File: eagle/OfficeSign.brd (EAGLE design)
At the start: 127.1 x 39.4 mm, 71 parts, among them Q1 16MHZ, SW3 KMR2, SW4 KMR2, U1 ATMEGA328, U2 L7805CDT-TR, U3 NCS36000, U4 PIR, U5 WS2801, U6 SPX3819, U8 TXB0108PWR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

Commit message: Move Files Around
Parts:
- removed U$10: FIDUCIAL, adafruit:FIDUCIAL_1MM
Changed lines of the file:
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@@
 <attribute name="SPICEPREFIX" value="C" x="46.355" y="27.178" size="1.778" layer="27" rot="R270" display="off"/>
 </element>
-<element name="U$10" library="adafruit" package="FIDUCIAL_1MM" value="FIDUCIAL" x="45.085" y="19.304"/>
 </elements>
 <signals>

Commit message: WIP
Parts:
- removed D11: MBR120, microbuilder:SOD-123
- added D2: MBR120, microbuilder:SOD-123
- moved D10 4.71 mm to (24.1, 32.0), turned to 90 degrees
- moved C16 1.80 mm to (43.8, 25.4), turned to 90 degrees
- moved C17 1.78 mm to (46.4, 25.4), turned to 90 degrees
- moved R10 0.80 mm to (125.5, 21.8)
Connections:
- net STROBE renamed D2
- removed net D5: U1.9
- removed net D6: U1.10
- removed net GPIO4: X2.13
- removed net GPIO5: X2.14
- removed net N$17: C15.1, D10.C, D11.C, R21.1, U6.1
- removed net RST7: U1.1
- removed net VBAT: D11.A
- new net N$23: C15.1, D10.C, D2.C, R21.1, U6.1
- new net OCC: U1.9, U8.15
- new net OCC_ESP: U8.6, X2.13
- new net RES: U1.10, U8.14
- new net RES_ESP: U8.7, X2.14
- net OUT: now also U1.1
- net VCC: now also D2.A
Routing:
- net N$23: track 0.00 -> 23.2 mm
- net N$17: track 22.2 -> 0.00 mm
- net VIN: track 29.8 -> 13.2 mm
- net GND: track 0.90 -> 0.00 mm
- net VBAT: track 0.54 -> 0.00 mm

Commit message: Moves and Shakes
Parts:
- added POT: (no value), SparkFun-Connectors:JST-4-PTH
- added R15: 3.3, adafruit:M0805
- added U7: NJVMJD2955T4G, bg_eagle_lib:DPAK
- C19: value 10uF -> 0.33uF
- moved JP1 10.2 mm to (76.6, 1.52)
- moved C2 8.98 mm to (86.9, 14.2)
- moved C19 8.89 mm to (96.9, 21.0)
- moved Q1 8.68 mm to (93.4, 29.8)
- moved C3 8.27 mm to (92.8, 25.7)
- moved R6 7.11 mm to (77.9, 32.3)
- moved R2 6.18 mm to (86.9, 19.1), turned to 90 degrees
- moved U1 5.91 mm to (84.3, 28.3)
- moved S1 5.86 mm to (80.1, 19.6)
- moved C1 4.83 mm to (77.6, 30.0)
- moved U2 3.31 mm to (101.6, 18.9)
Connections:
- new net N$24: POT.3
- new net N$25: POT.2
- new net N$26: JP4.PWR, R15.2, U7.3
- net GND: now also POT.1
- net RAW: now also R15.1, U7.1; no longer JP4.PWR
- net VCC: now also POT.4, U7.4

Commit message: Add Indicator
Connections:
- removed net A1: U1.24
- removed net N$24: POT.3
- new net POT: POT.3, U1.24
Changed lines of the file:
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@@
 <?xml version="1.0" encoding="utf-8"?>
 <!DOCTYPE eagle SYSTEM "eagle.dtd">
-<eagle version="8.7.0">
+<eagle version="8.7.1">
 <drawing>
 <settings>
@@
 <contactref element="U1" pad="13"/>
 </signal>
-<signal name="A1">
+<signal name="POT">
 <contactref element="U1" pad="24"/>
+<contactref element="POT" pad="3"/>
+<wire x1="97.012" y1="6.096" x2="79.312771875" y2="29.376425" width="0" layer="19" extent="1-1"/>
 </signal>
 <signal name="D4">
@@
 <wire x1="24.13" y1="30.154" x2="26.416" y2="30.154" width="0.4064" layer="1"/>
 </signal>
-<signal name="N$24">
-<contactref element="POT" pad="3"/>
-</signal>
 <signal name="N$25">

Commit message: wip
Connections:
- net D2 renamed POD_IND
- net N$25 renamed POT_IND
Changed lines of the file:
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@@
 <wire x1="48.0028" y1="18.329" x2="88.7775375" y2="29.9421125" width="0" layer="19" extent="1-1"/>
 </signal>
-<signal name="D2">
+<signal name="POD_IND">
 <contactref element="U1" pad="32"/>
 </signal>
@@
 <wire x1="24.13" y1="30.154" x2="26.416" y2="30.154" width="0.4064" layer="1"/>
 </signal>
-<signal name="N$25">
+<signal name="POT_IND">
 <contactref element="POT" pad="2"/>
 </signal>

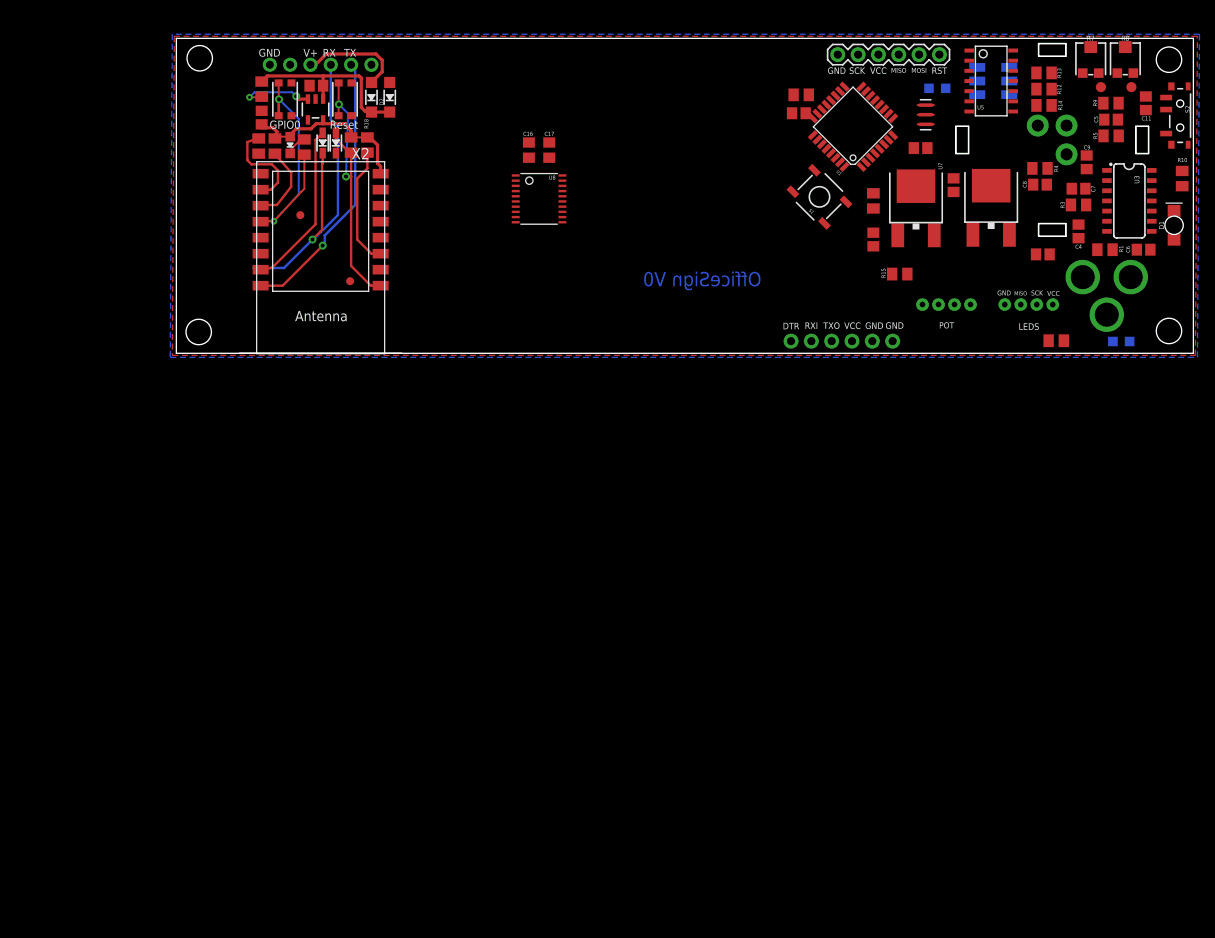
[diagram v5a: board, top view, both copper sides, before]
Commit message: Add Remote Motion / Work on Dispaly
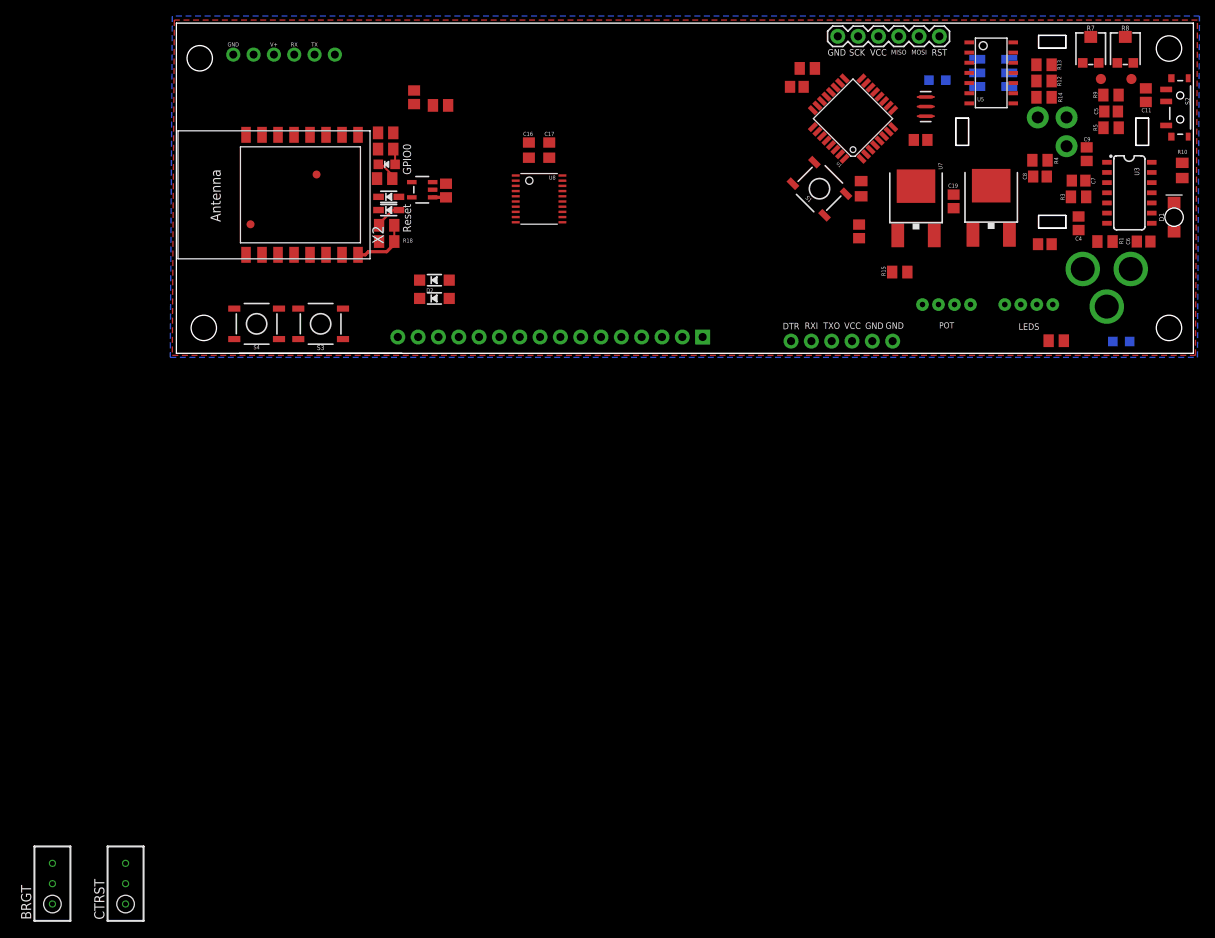
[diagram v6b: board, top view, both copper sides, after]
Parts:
- removed SW3, SW4: KMR2, microbuilder:BTN_KMR2_4.6X2.8
- added BRGT: 1K, resistor:RTRIM3296W
- added CTRST: 10K, resistor:RTRIM3296W
- added S3: Reset, SparkFun-Switches:TACTILE_SWITCH_SMD_5.2MM
- added S4: GPIO0, SparkFun-Switches:TACTILE_SWITCH_SMD_5.2MM
- added U9: LCD-16X2NOHOLES, SparkFun-Displays:LCD-16X2_NOHOLES
- S1: device Testing:TACTILE-SWITCH-SMD-ALT01 -> SparkFun-Switches:TACTILE_SWITCH_SMD_5.2MM
- moved D2 25.8 mm to (32.0, 6.86), turned to 0 degrees
- moved D10 24.2 mm to (32.0, 9.14), turned to 0 degrees
- moved R21 22.4 mm to (32.8, 31.0), turned to 180 degrees
- moved U$34 21.3 mm to (7.49, 28.7), turned to 270 degrees
- moved C15 20.8 mm to (33.5, 20.3), turned to 90 degrees
- moved C14 19.2 mm to (29.5, 32.0)
- moved U6 16.7 mm to (30.5, 20.4), turned to 90 degrees
- moved R20 16.0 mm to (25.9, 27.6), turned to 0 degrees
- moved FID2 14.3 mm to (9.02, 16.1), turned to 90 degrees
- moved R22 13.8 mm to (25.9, 25.5), turned to 0 degrees
- moved D12 12.3 mm to (26.0, 23.6), turned to 90 degrees
- moved R18 12.3 mm to (26.0, 14.0), turned to 0 degrees
- moved R19 11.0 mm to (26.0, 16.0), turned to 0 degrees
- moved R23 10.8 mm to (25.8, 21.8), turned to 0 degrees
- moved D8 10.7 mm to (26.3, 17.9), turned to 0 degrees
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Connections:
- net POD_IND renamed D2
- removed net N$26: JP4.PWR, R15.2, U7.3
- removed net POT_IND: POT.2
- removed net SSRX: U1.12
- new net A1: BRGT.2, U9.15
- new net DB4: U9.11
- new net DB5: U9.12
- new net DB6: U9.13
- new net DB7: U9.14
- new net E: U9.6
- new net L7805_IN: C19.1, R15.1, U2.1, U7.1
- new net POT_LED: POT.2, U1.1
- new net RS: U9.4
- new net VO: CTRST.2, U9.3
- net GND: now also CTRST.1, S3.1, S3.2, S4.1, S4.2, U9.1, U9.16, U9.5; no longer SW3.A, SW3.A', SW4.A, SW4.A'
- net GPIO0: now also S4.3, S4.4; no longer SW4.B, SW4.B'
- net OUT: now also U1.12; no longer U1.1
- net RAW: now also JP4.PWR, R15.2, U7.3; no longer C19.1, LEDS.4, R15.1, U2.1, U7.1
- net RESET_HZA: now also S3.3, S3.4; no longer SW3.B, SW3.B'
- net VCC: now also BRGT.3, CTRST.3, LEDS.4, U9.2
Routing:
- net RXD_5V: track 43.8 -> 0.00 mm, vias 1 -> 0
- net GPIO0: track 35.2 -> 0.00 mm, vias 2 -> 0
- net TXD: track 35.3 -> 1.02 mm, vias 1 -> 0
- net RESET_HZA: track 36.5 -> 3.38 mm, vias 2 -> 0
- net N$23: track 23.2 -> 1.67 mm
- net RXD: track 20.9 -> 0.00 mm
- net CH_PD: track 15.0 -> 0.00 mm
- net 3.3V: track 23.0 -> 9.48 mm
- net VIN: track 13.2 -> 0.00 mm
- net GPIO15: track 12.0 -> 0.00 mm
- net GPIO2: track 9.75 -> 0.00 mm
- net LDO_EN: track 9.46 -> 0.00 mm, vias 2 -> 0
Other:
- board size 127.1 x 39.4 mm -> 127.1 x 41.3 mm
- board text added: "LED"
- board text added: "LED MAX: 1.5A"
- board text added: "LEDS"
- board text added: "POT"
- board text added: "VCC: 9-12V"
- board text removed: "OfficeSign V0"

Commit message: Add Display / Add Indicator LEDs
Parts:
- removed D12: RED, microbuilder:CHIPLED_0805_NOOUTLINE
- added D4: Green, led:CHIPLED_0805
- added D5: Red, led:CHIPLED_0805
- added LED3: RED, led:CHIP-LED0805
- added R16: 1k, adafruit:M0805
- added R17: 300, adafruit:M0805
- D1: device SparkFun-LED:LED-1206-BOTTOM -> led:CHIPLED_0805
- D3, LED1: device adafruit:CHIPLED_0805 -> led:CHIPLED_0805
- moved CTRST 113.8 mm to (79.0, 8.64), turned to 270 degrees
- moved BRGT 95.4 mm to (42.9, 8.89), turned to 90 degrees
- moved FRAME1 65.2 mm to (48.3, -53.3)
- moved JP1 38.3 mm to (72.3, 39.6), turned to 0 degrees
- moved U9 16.8 mm to (50.3, -13.7)
- moved D1 5.98 mm to (123.2, 22.9), flipped to the bottom, turned to 0 degrees
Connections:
- removed net DB4: U9.11
- removed net DB5: U9.12
- removed net DB6: U9.13
- removed net DB7: U9.14
- removed net GPIO12: X2.6
- removed net GPIO13: X2.7
- removed net GPIO14: X2.5
- removed net GPIO15: R20.2, X2.10
- removed net GPIO16: X2.4
- removed net GPIO2: R22.1, X2.11
- removed net RS: U9.4
- new net E_ESP: R22.1, U8.3, X2.11
- new net LCD4_ESP: U8.4, X2.4
- new net LCD5_ESP: U8.5, X2.5
- new net LCD6_ESP: U8.6, X2.6
- new net LCD7_ESP: U8.7, X2.7
- new net LCD_D4: U8.17, U9.11
- new net LCD_D5: U8.16, U9.12
- new net LCD_D6: U8.15, U9.13
- new net LCD_D7: U8.14, U9.14
- new net LCD_E: U9.6
- new net LCD_RS: U8.20, U9.4
- new net N$17: LED3.C, R23.2
- new net N$24: D4.C, R16.2
- new net RS_ESP: R20.2, U8.1, X2.10
- net 3.3V: now also LED3.A; no longer D12.A
- net E: now also U8.18; no longer U9.6
- net GND: now also R16.1, R17.1
- net N$18: now also D5.C, R17.2; no longer D12.C, R23.2
- net OCC: now also D4.A, U8.13; no longer U8.15
- net OCC_ESP: now also U8.8; no longer U8.6
- net RES: now also U8.12; no longer U8.14
- net RES_ESP: now also D5.A, U8.9; no longer U8.7
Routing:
- net N$18: track 3.22 -> 0.00 mm
- net 3.3V: track 9.48 -> 8.06 mm
- net LCD5_ESP: track 0.00 -> 0.83 mm
- net GPIO14: track 0.83 -> 0.00 mm

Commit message: Screen is plugged in but doesnt work
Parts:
- R15: value 3.3 -> 22
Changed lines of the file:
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@@
 <attribute name="VALUE" x="88.646" y="16.618" size="0.508" layer="27" rot="R90"/>
 </element>
-<element name="R15" library="adafruit" package="M0805" value="3.3" x="90.17" y="10.16" smashed="yes">
+<element name="R15" library="adafruit" package="M0805" value="22" x="90.17" y="10.16" smashed="yes">
 <attribute name="NAME" x="88.392" y="9.652" size="0.508" layer="25" rot="R90"/>
 <attribute name="VALUE" x="92.456" y="9.652" size="0.508" layer="27" rot="R90"/>
